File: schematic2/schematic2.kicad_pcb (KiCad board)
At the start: 2 copper layers, 68.8 x 56 mm, 46 parts, among them J1 Barrel_Jack, K1 TIANBO_HJR_1-2C, P1 Conn_02x20_Odd_Even, Q1 BC547, Q2 BC557, Q3 BC547, Q4 BC547, U1 buck, U2 DS3231M, U3 MCP1700-1202E_SOT89

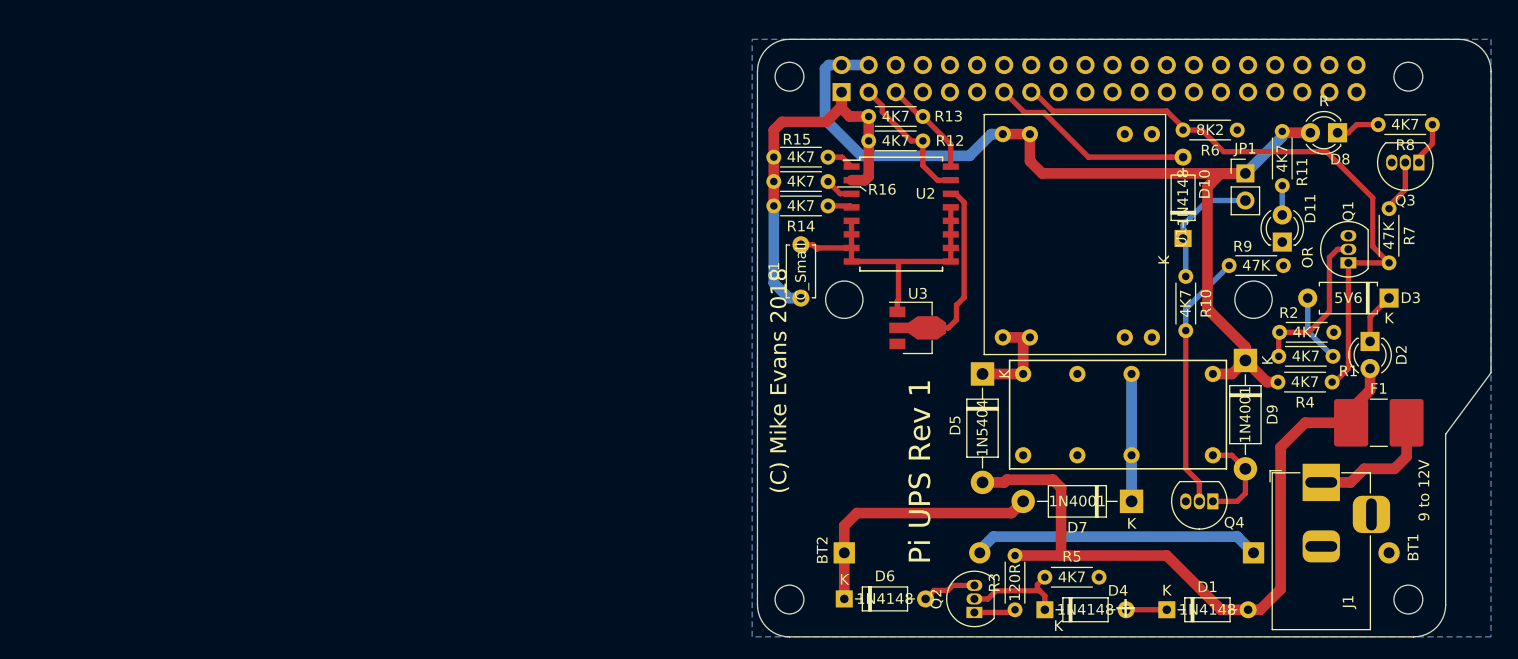
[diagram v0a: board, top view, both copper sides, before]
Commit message: Added EEPROM
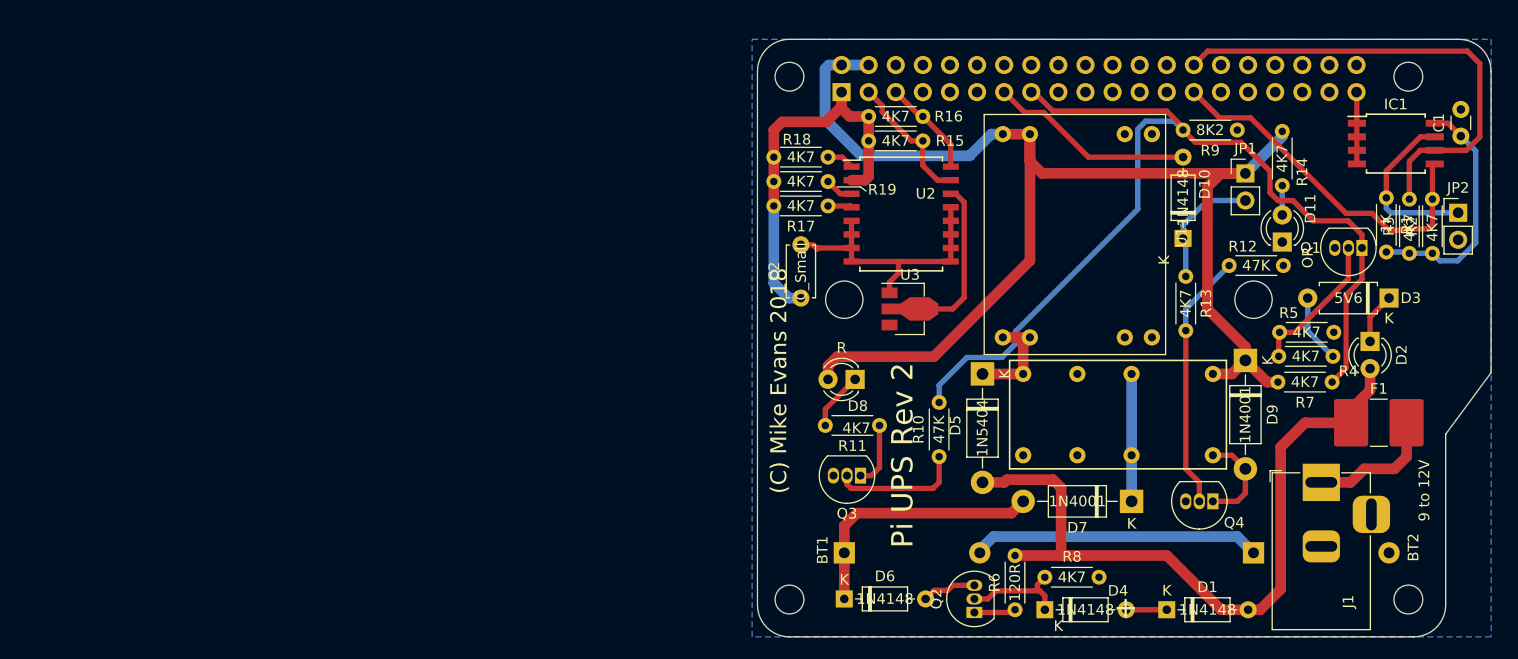
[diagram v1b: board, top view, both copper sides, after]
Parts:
- added C1: 0.1uF, Capacitor_THT:C_Disc_D3.0mm_W1.6mm_P2.50mm, F.Cu at (266.4, 103.1)
- added IC1: CAT24C32WI-GT3, Package_SO:SOIJ-8_5.3x5.3mm_P1.27mm, F.Cu at (260.3, 103.8)
- added JP2: Jumper_NO_Small, Connector_PinHeader_2.54mm:PinHeader_1x02_P2.54mm_Vertical, F.Cu at (266.2, 110.2)
- added R1: 1K, Resistor_THT:R_Axial_DIN0204_L3.6mm_D1.6mm_P5.08mm_Horizontal, F.Cu at (259.4, 108.9)
- added R2: 4K7, Resistor_THT:R_Axial_DIN0204_L3.6mm_D1.6mm_P5.08mm_Horizontal, F.Cu at (263.8, 114.1)
- added R3: 4K7, Resistor_THT:R_Axial_DIN0204_L3.6mm_D1.6mm_P5.08mm_Horizontal, F.Cu at (261.6, 114.1)
- moved Q3 60.0 mm to (210.2, 134.9)
- moved R11 59.0 mm to (211.9, 130.2)
- moved D8 50.8 mm to (209.7, 125.9)
- moved R10 48.1 mm to (217.5, 133.1), turned to 90 degrees
- moved U3 1.92 mm to (214.4, 119.3)
- moved Q1 1.89 mm to (257.1, 113.6), turned to 180 degrees
- renumbered BT2 to BT1, BT1 to BT2, C1 to C2, R7 to R10, R8 to R11, R9 to R12, R10 to R13, R11 to R14, R12 to R15, R13 to R16, R14 to R17, R15 to R18, R16 to R19, R1 to R4, R2 to R5, R3 to R6, R4 to R7, R5 to R8, R6 to R9
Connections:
- P1 pad 27: /ID_SD -> ID_SD
- P1 pad 28: /ID_SC -> ID_SC
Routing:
- net ID_SC: track 0.00 -> 45.8 mm
- net POWER_FAIL: track 58.9 -> 93.1 mm
- net ID_SD: track 0.00 -> 33.7 mm
- net +5V: track 90.4 -> 123.9 mm
- net +3.3V: track 0.00 -> 22.9 mm
- net Net-(IC1-Pad7): track 0.00 -> 16.3 mm
- net Net-(Q3-Pad2): track 4.95 -> 12.3 mm
- net GND: track 27.9 -> 33.2 mm
- net Net-(Q3-Pad1): track 4.08 -> 6.04 mm
- net Net-(D8-Pad1): track 4.13 -> 5.48 mm
- net Net-(Q1-Pad2): track 14.9 -> 13.7 mm
- net Net-(U2-Pad14): track 18.6 -> 17.8 mm
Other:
- board text added: "Pi UPS Rev 2"
- board text removed: "Pi UPS Rev 1"

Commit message: Fix wrongly connected clock battery reg
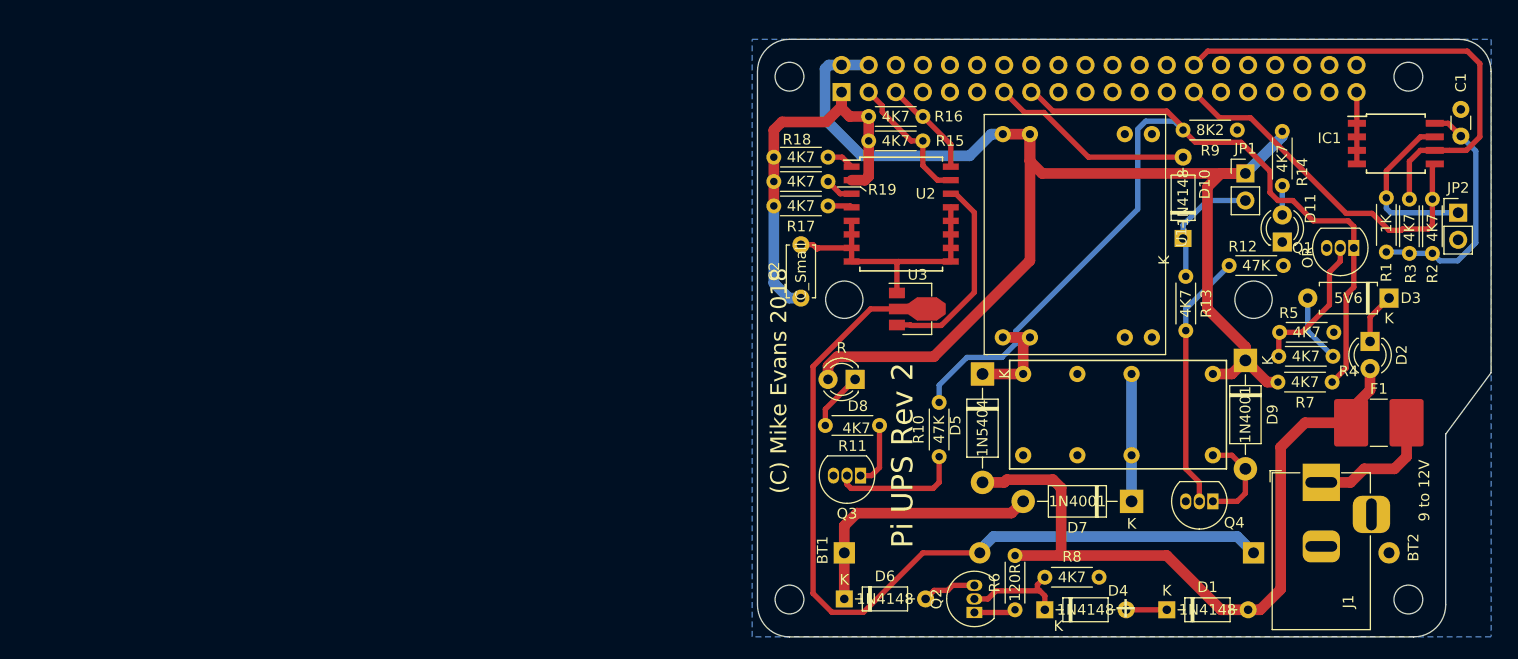
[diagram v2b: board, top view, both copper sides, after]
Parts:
- moved Q1 0.76 mm to (256.4, 113.6)
- moved U3 0.70 mm to (215.0, 119.3)
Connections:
- BT1 pad 2: Net-(BT1-Pad2) -> /Sheet5B4BA297/VI
- BT2 pad 1: Net-(BT1-Pad2) -> /Sheet5B4BA297/VI
- U3 pad 2: Net-(U2-Pad14) -> /Sheet5B4BA297/VI
- U3 pad 3: /Sheet5B4BA297/V0 -> Net-(U2-Pad14)
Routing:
- net /Sheet5B4BA297/VI: track 0.00 -> 81.2 mm
- net Net-(BT1-Pad2): track 27.1 -> 0.00 mm
- net Net-(U2-Pad14): track 17.8 -> 19.0 mm
- net POWER_FAIL: track 93.1 -> 92.4 mm

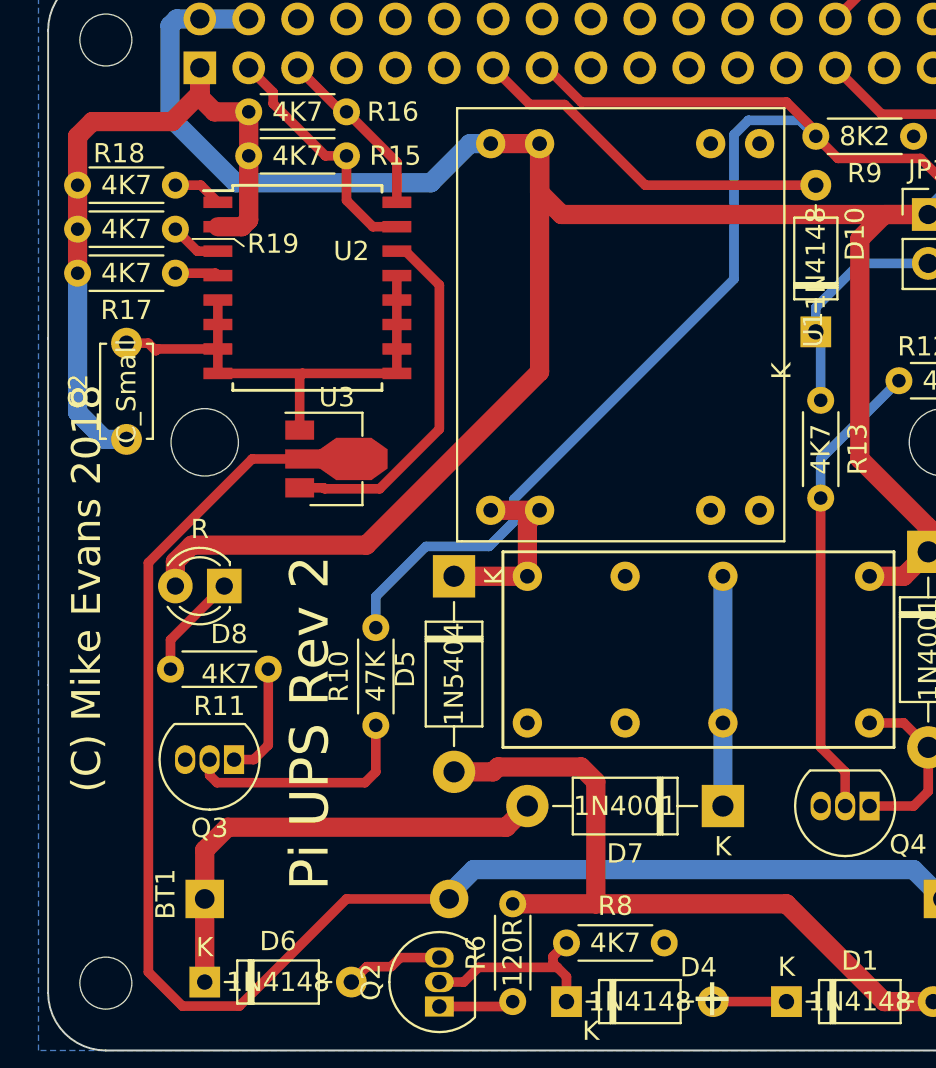
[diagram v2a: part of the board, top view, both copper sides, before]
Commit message: Fix wron wiring to clock.
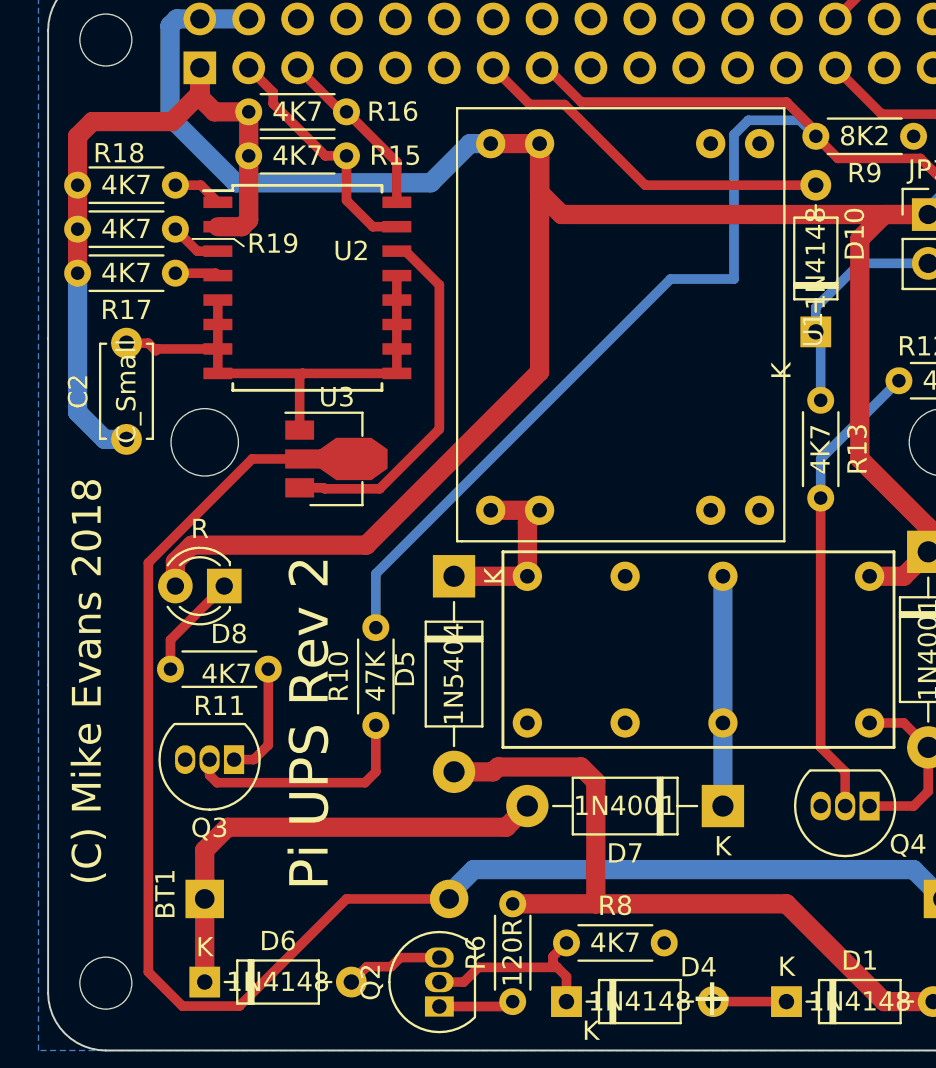
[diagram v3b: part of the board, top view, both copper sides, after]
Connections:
- JP2 pad 1: Net-(IC1-Pad7) -> Net-(JP2-Pad1)
- JP2 pad 2: GND -> Net-(JP2-Pad2)
- R2 pad 1: +3.3V -> Net-(R2-Pad1)
- R3 pad 1: +3.3V -> Net-(R3-Pad1)
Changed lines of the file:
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@@
     (thickness 1.6)
     (drawings 34)
-    (tracks 257)
+    (tracks 254)
     (zones 0)
     (modules 52)
-    (nets 62)
+    (nets 66)
   )
   (page A3)
@@
   (net 60 "Net-(R19-Pad1)")
   (net 61 /Sheet5B4BA297/VI)
+  (net 62 "Net-(JP2-Pad1)")
+  (net 63 "Net-(JP2-Pad2)")
+  (net 64 "Net-(R2-Pad1)")
+  (net 65 "Net-(R3-Pad1)")
   (net_class Default "This is the default net class."
     (clearance 0.2)
@@
     (add_net "Net-(D9-Pad2)")
     (add_net "Net-(IC1-Pad7)")
+    (add_net "Net-(JP2-Pad1)")
+    (add_net "Net-(JP2-Pad2)")
     (add_net "Net-(K1-Pad11)")
     (add_net "Net-(K1-Pad6)")
@@
     (add_net "Net-(R18-Pad1)")
     (add_net "Net-(R19-Pad1)")
+    (add_net "Net-(R2-Pad1)")
+    (add_net "Net-(R3-Pad1)")
     (add_net "Net-(U2-Pad14)")
     (add_net PI_P_SIG)
@@
     )
     (pad 1 thru_hole rect (at 0 0) (size 1.7 1.7) (drill 1) (layers *.Cu *.Mask)
-      (net 54 "Net-(IC1-Pad7)"))
+      (net 62 "Net-(JP2-Pad1)"))
     (pad 2 thru_hole oval (at 0 2.54) (size 1.7 1.7) (drill 1) (layers *.Cu *.Mask)
-      (net 2 GND))
+      (net 63 "Net-(JP2-Pad2)"))
     (model ${KISYS3DMOD}/Connector_PinHeader_2.54mm.3dshapes/PinHeader_1x02_P2.54mm_Vertical.wrl
       (at (xyz 0 0 0))
@@
     )
     (pad 1 thru_hole circle (at 0 0 90) (size 1.4 1.4) (drill 0.7) (layers *.Cu *.Mask)
-      (net 57 +3.3V))
+      (net 64 "Net-(R2-Pad1)"))
     (pad 2 thru_hole oval (at 5.08 0 90) (size 1.4 1.4) (drill 0.7) (layers *.Cu *.Mask)
       (net 55 ID_SD))
@@
       (net 56 ID_SC))
     (pad 1 thru_hole circle (at 0 0 90) (size 1.4 1.4) (drill 0.7) (layers *.Cu *.Mask)
-      (net 57 +3.3V))
+      (net 65 "Net-(R3-Pad1)"))
     (model ${KISYS3DMOD}/Resistor_THT.3dshapes/R_Axial_DIN0204_L3.6mm_D1.6mm_P5.08mm_Horizontal.wrl
       (at (xyz 0 0 0))
@@
     (effects (font (size 2 2) (thickness 0.22225)))
   )
-  (gr_text "(C) Mike Evans 2018" (at 202.5 126 90) (layer F.SilkS)
+  (gr_text "(C) Mike Evans 2018" (at 202.54 130.823 90) (layer F.SilkS)
     (effects (font (size 1.5 1.5) (thickness 0.25)))
   )
@@
   (segment (start 238.862 100.724) (end 228.194 100.724) (width 0.5) (layer F.Cu) (net 10))
   (segment (start 240.386 102.248) (end 238.862 100.724) (width 0.5) (layer F.Cu) (net 10) (status 400010))
-  (segment (start 217.526 126.415998) (end 217.526 128.029) (width 0.5) (layer B.Cu) (net 10) (status 20))
-  (segment (start 220.129999 123.811999) (end 217.526 126.415998) (width 0.5) (layer B.Cu) (net 10))
-  (segment (start 223.409763 123.811999) (end 220.129999 123.811999) (width 0.5) (layer B.Cu) (net 10))
-  (segment (start 224.707001 122.514761) (end 223.409763 123.811999) (width 0.5) (layer B.Cu) (net 10))
-  (segment (start 224.707001 121.351239) (end 224.707001 122.514761) (width 0.5) (layer B.Cu) (net 10))
-  (segment (start 236.137001 109.921239) (end 224.707001 121.351239) (width 0.5) (layer B.Cu) (net 10))
-  (segment (start 236.137001 102.417237) (end 236.137001 109.921239) (width 0.5) (layer B.Cu) (net 10))
-  (segment (start 236.883239 101.670999) (end 236.137001 102.417237) (width 0.5) (layer B.Cu) (net 10))
-  (segment (start 239.554999 101.670999) (end 236.883239 101.670999) (width 0.5) (layer B.Cu) (net 10))
-  (segment (start 240.386 102.502) (end 239.554999 101.670999) (width 0.5) (layer B.Cu) (net 10) (status 10))
   (segment (start 255.664001 124.815999) (end 255.664001 117.957999) (width 0.5) (layer F.Cu) (net 10))
   (segment (start 254.356 126.124) (end 255.664001 124.815999) (width 0.5) (layer F.Cu) (net 10) (status 10))
@@
   (segment (start 256.388 117.234) (end 256.388 113.551) (width 0.5) (layer F.Cu) (net 10))
   (segment (start 255.664001 117.957999) (end 256.388 117.234) (width 0.5) (layer F.Cu) (net 10))
+  (segment (start 217.526 125.235) (end 232.839761 109.921239) (width 0.5) (layer B.Cu) (net 10))
+  (segment (start 236.137001 102.417237) (end 236.883239 101.670999) (width 0.5) (layer B.Cu) (net 10))
+  (segment (start 217.526 128.029) (end 217.526 125.235) (width 0.5) (layer B.Cu) (net 10))
+  (segment (start 232.839761 109.921239) (end 236.137001 109.921239) (width 0.5) (layer B.Cu) (net 10))
+  (segment (start 239.554999 101.670999) (end 240.386 102.502) (width 0.5) (layer B.Cu) (net 10))
+  (segment (start 236.137001 109.921239) (end 236.137001 102.417237) (width 0.5) (layer B.Cu) (net 10))
+  (segment (start 236.883239 101.670999) (end 239.554999 101.670999) (width 0.5) (layer B.Cu) (net 10))
   (segment (start 235.56 137.3) (end 235.56 132.982) (width 1) (layer B.Cu) (net 11) (status C00030))
   (segment (start 235.56 132.982) (end 235.56 125.362) (width 1) (layer B.Cu) (net 11) (status C00030))
@@
   (segment (start 219.07 108.471) (end 218.62 108.471) (width 0.5) (layer F.Cu) (net 26))
   (segment (start 220.828 117.715912) (end 220.828 110.229) (width 0.5) (layer F.Cu) (net 26))
-  (segment (start 213.0175 119.266) (end 217.018 119.266) (width 0.5) (layer F.Cu) (net 61) (status 30))
   (segment (start 221.59 125.362) (end 225.4 125.362) (width 1) (layer F.Cu) (net 53) (status 30))
   (segment (start 223.495 121.933) (end 226.035 121.933) (width 1) (layer F.Cu) (net 53) (status 30))
   (segment (start 225.4 122.568) (end 226.035 121.933) (width 1) (layer F.Cu) (net 53) (status 20))
   (segment (start 225.4 125.362) (end 225.4 122.568) (width 1) (layer F.Cu) (net 53) (status 10))
-  (segment (start 221.336 142.126) (end 221.336 141.872) (width 1) (layer B.Cu) (net 61) (status C00030))
-  (segment (start 245.466 140.602) (end 246.99 142.126) (width 1) (layer B.Cu) (net 61) (status 800020))
-  (segment (start 222.606 140.602) (end 245.466 140.602) (width 1) (layer B.Cu) (net 61))
-  (segment (start 221.336 141.872) (end 222.606 140.602) (width 1) (layer B.Cu) (net 61) (status 400010))
   (segment (start 262.625 103.137) (end 263.975 103.137) (width 0.5) (layer F.Cu) (net 54))
   (segment (start 259.436 106.326) (end 262.625 103.137) (width 0.5) (layer F.Cu) (net 54))
@@
   (segment (start 208.255 108.471) (end 209.32 108.471) (width 0.5) (layer F.Cu) (net 60) (status 20))
   (segment (start 207.112 107.328) (end 208.255 108.471) (width 0.5) (layer F.Cu) (net 60) (status 10))
+  (segment (start 213.0175 119.266) (end 217.018 119.266) (width 0.5) (layer F.Cu) (net 61) (status 30))
+  (segment (start 221.336 142.126) (end 221.336 141.872) (width 1) (layer B.Cu) (net 61) (status C00030))
+  (segment (start 245.466 140.602) (end 246.99 142.126) (width 1) (layer B.Cu) (net 61) (status 800020))
+  (segment (start 222.606 140.602) (end 245.466 140.602) (width 1) (layer B.Cu) (net 61))
+  (segment (start 221.336 141.872) (end 222.606 140.602) (width 1) (layer B.Cu) (net 61) (status 400010))
   (segment (start 207.475999 147.694001) (end 210.433999 147.694001) (width 0.5) (layer F.Cu) (net 61))
   (segment (start 205.707999 145.926001) (end 207.475999 147.694001) (width 0.5) (layer F.Cu) (net 61))
